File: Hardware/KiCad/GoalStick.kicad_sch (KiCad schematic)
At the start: 0 parts

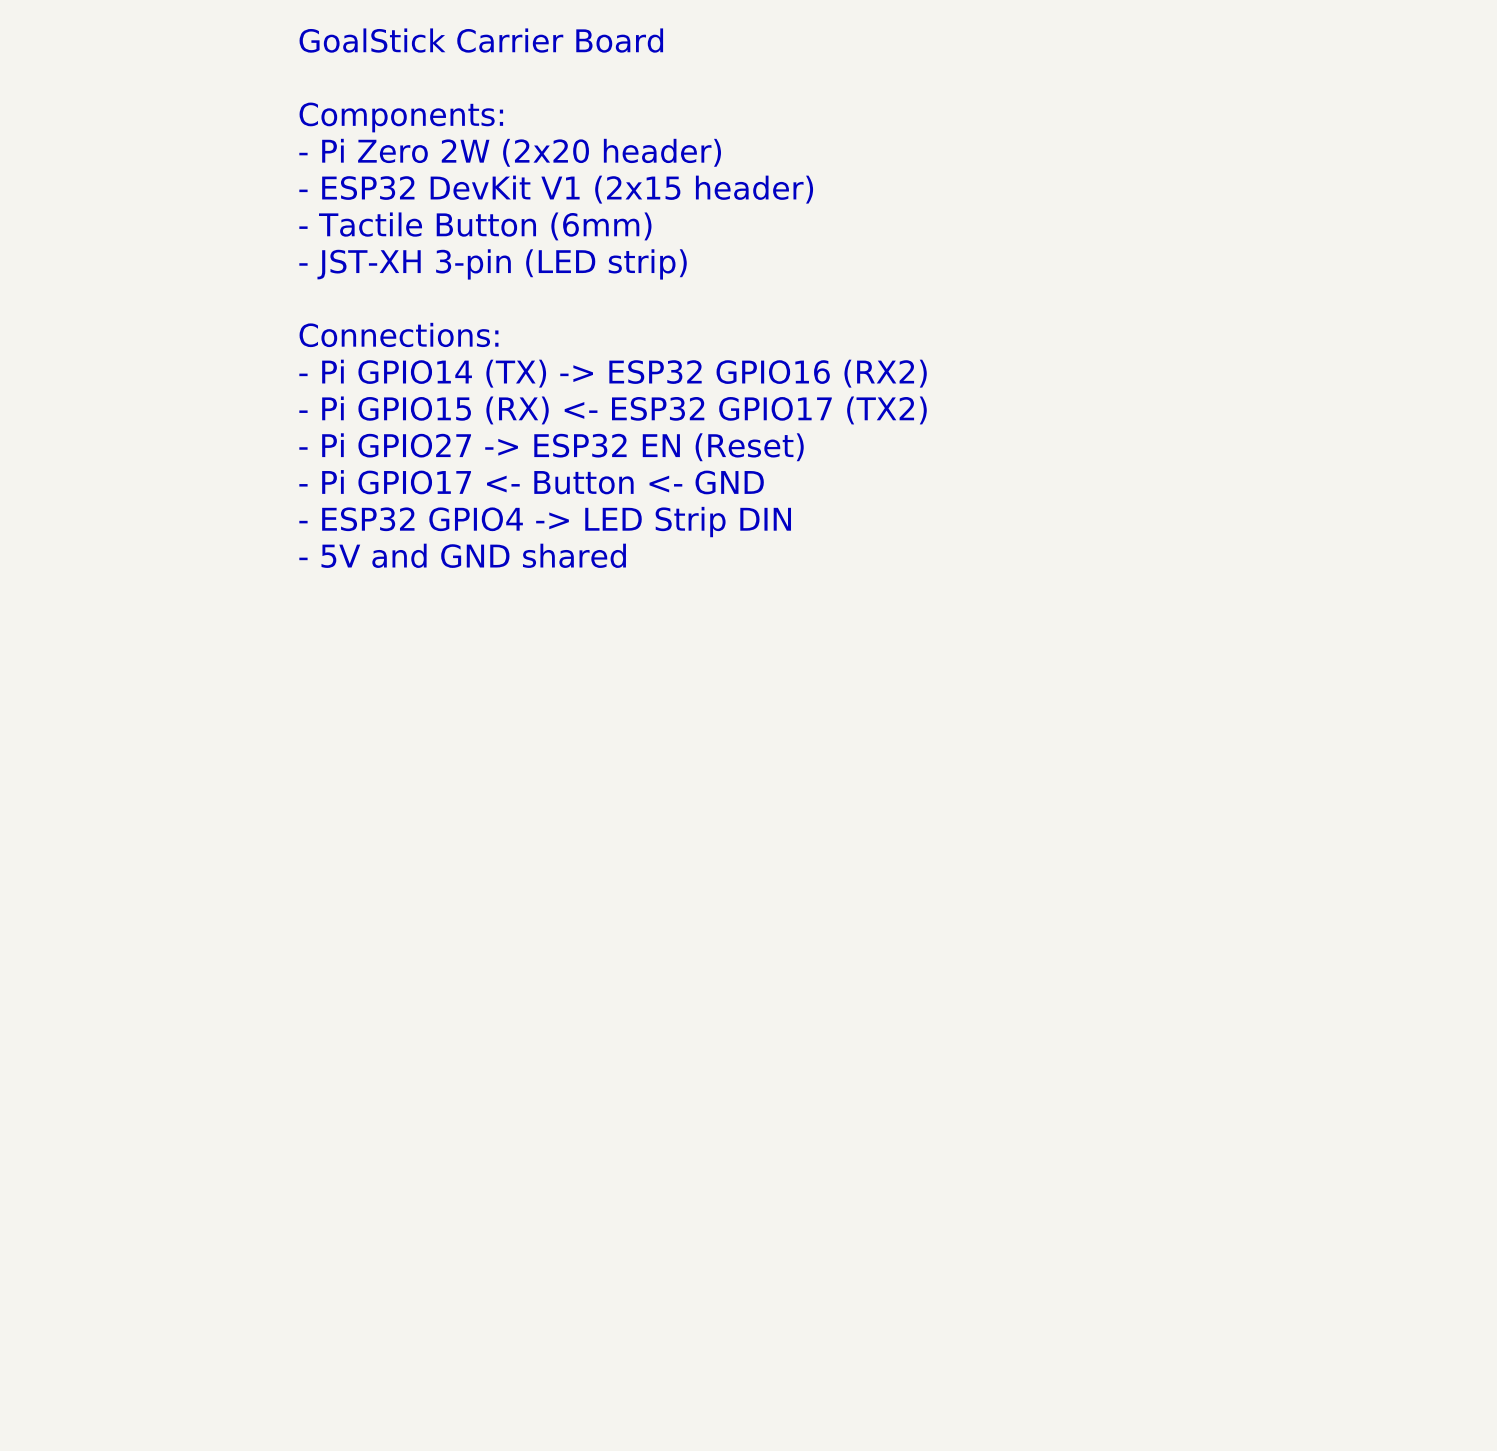
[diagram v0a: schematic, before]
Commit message: Add KiCad PCB design for GoalStick carrier board
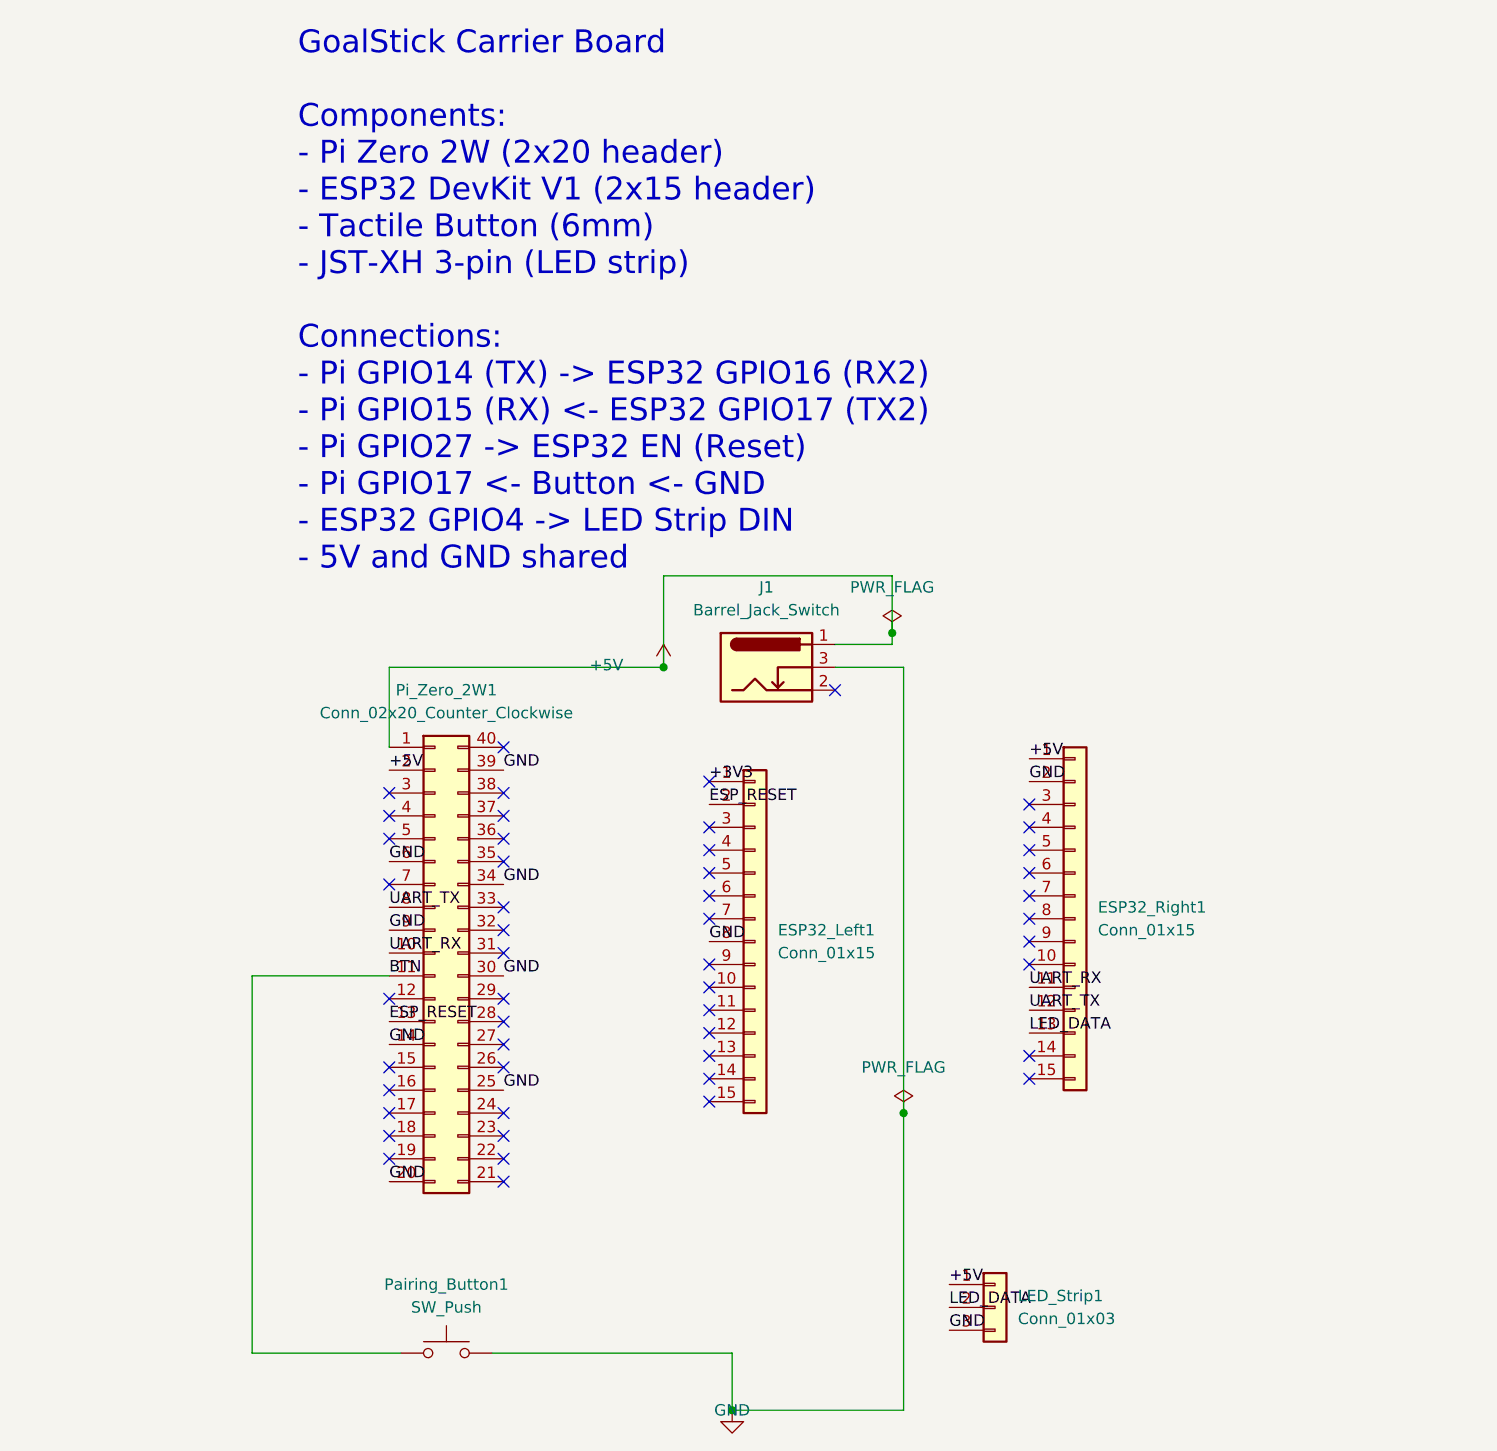
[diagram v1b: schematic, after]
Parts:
- added ESP32_Left1, ESP32_Right1: Conn_01x15, Connector_PinSocket_2.54mm:PinSocket_1x15_P2.54mm_Vertical, symbol Connector_Generic:Conn_01x15
- added J1: Barrel_Jack_Switch, Connector_BarrelJack:BarrelJack_Horizontal, symbol Connector:Barrel_Jack_Switch
- added LED_Strip1: Conn_01x03, Connector_JST:JST_XH_B3B-XH-A_1x03_P2.50mm_Vertical, symbol Connector_Generic:Conn_01x03
- added Pairing_Button1: SW_Push, Button_Switch_THT:SW_PUSH_6mm, symbol Switch:SW_Push
- added Pi_Zero_2W1: Conn_02x20_Counter_Clockwise, Connector_PinSocket_2.54mm:PinSocket_2x20_P2.54mm_Vertical, symbol Connector_Generic:Conn_02x20_Counter_Clockwise
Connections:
- new net +3V3: ESP32_Left1.1 (Pin_1)
- new net +5V: ESP32_Right1.1 (Pin_1), J1.1, LED_Strip1.1 (Pin_1), Pi_Zero_2W1.1 (Pin_1), Pi_Zero_2W1.2 (Pin_2)
- new net BTN: Pairing_Button1.1, Pi_Zero_2W1.11 (Pin_11)
- new net ESP_RESET: ESP32_Left1.2 (Pin_2), Pi_Zero_2W1.13 (Pin_13)
- new net GND: ESP32_Left1.8 (Pin_8), ESP32_Right1.2 (Pin_2), J1.3, LED_Strip1.3 (Pin_3), Pairing_Button1.2, Pi_Zero_2W1.14 (Pin_14), Pi_Zero_2W1.20 (Pin_20), Pi_Zero_2W1.25 (Pin_25), Pi_Zero_2W1.30 (Pin_30), Pi_Zero_2W1.34 (Pin_34), Pi_Zero_2W1.39 (Pin_39), Pi_Zero_2W1.6 (Pin_6), Pi_Zero_2W1.9 (Pin_9)
- new net LED_DATA: ESP32_Right1.13 (Pin_13), LED_Strip1.2 (Pin_2)
- new net UART_RX: ESP32_Right1.11 (Pin_11), Pi_Zero_2W1.10 (Pin_10)
- new net UART_TX: ESP32_Right1.12 (Pin_12), Pi_Zero_2W1.8 (Pin_8)
- no-connect marks 0 -> 50

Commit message: Add DEPLOYMENT.md, update ESP32 firmware for XIAO ESP32C3, add KiCad footprints
- Add DEPLOYMENT.md with hands-free installation instructions
- Update README.md to link to deployment guide
- Update ESP32 firmware for XIAO ESP32C3 (Serial1, pin mappings, startup delay)
- Add custom KiCad footprints for XIAO and Pi Zero 2W
- Update KiCad schematic and PCB layout
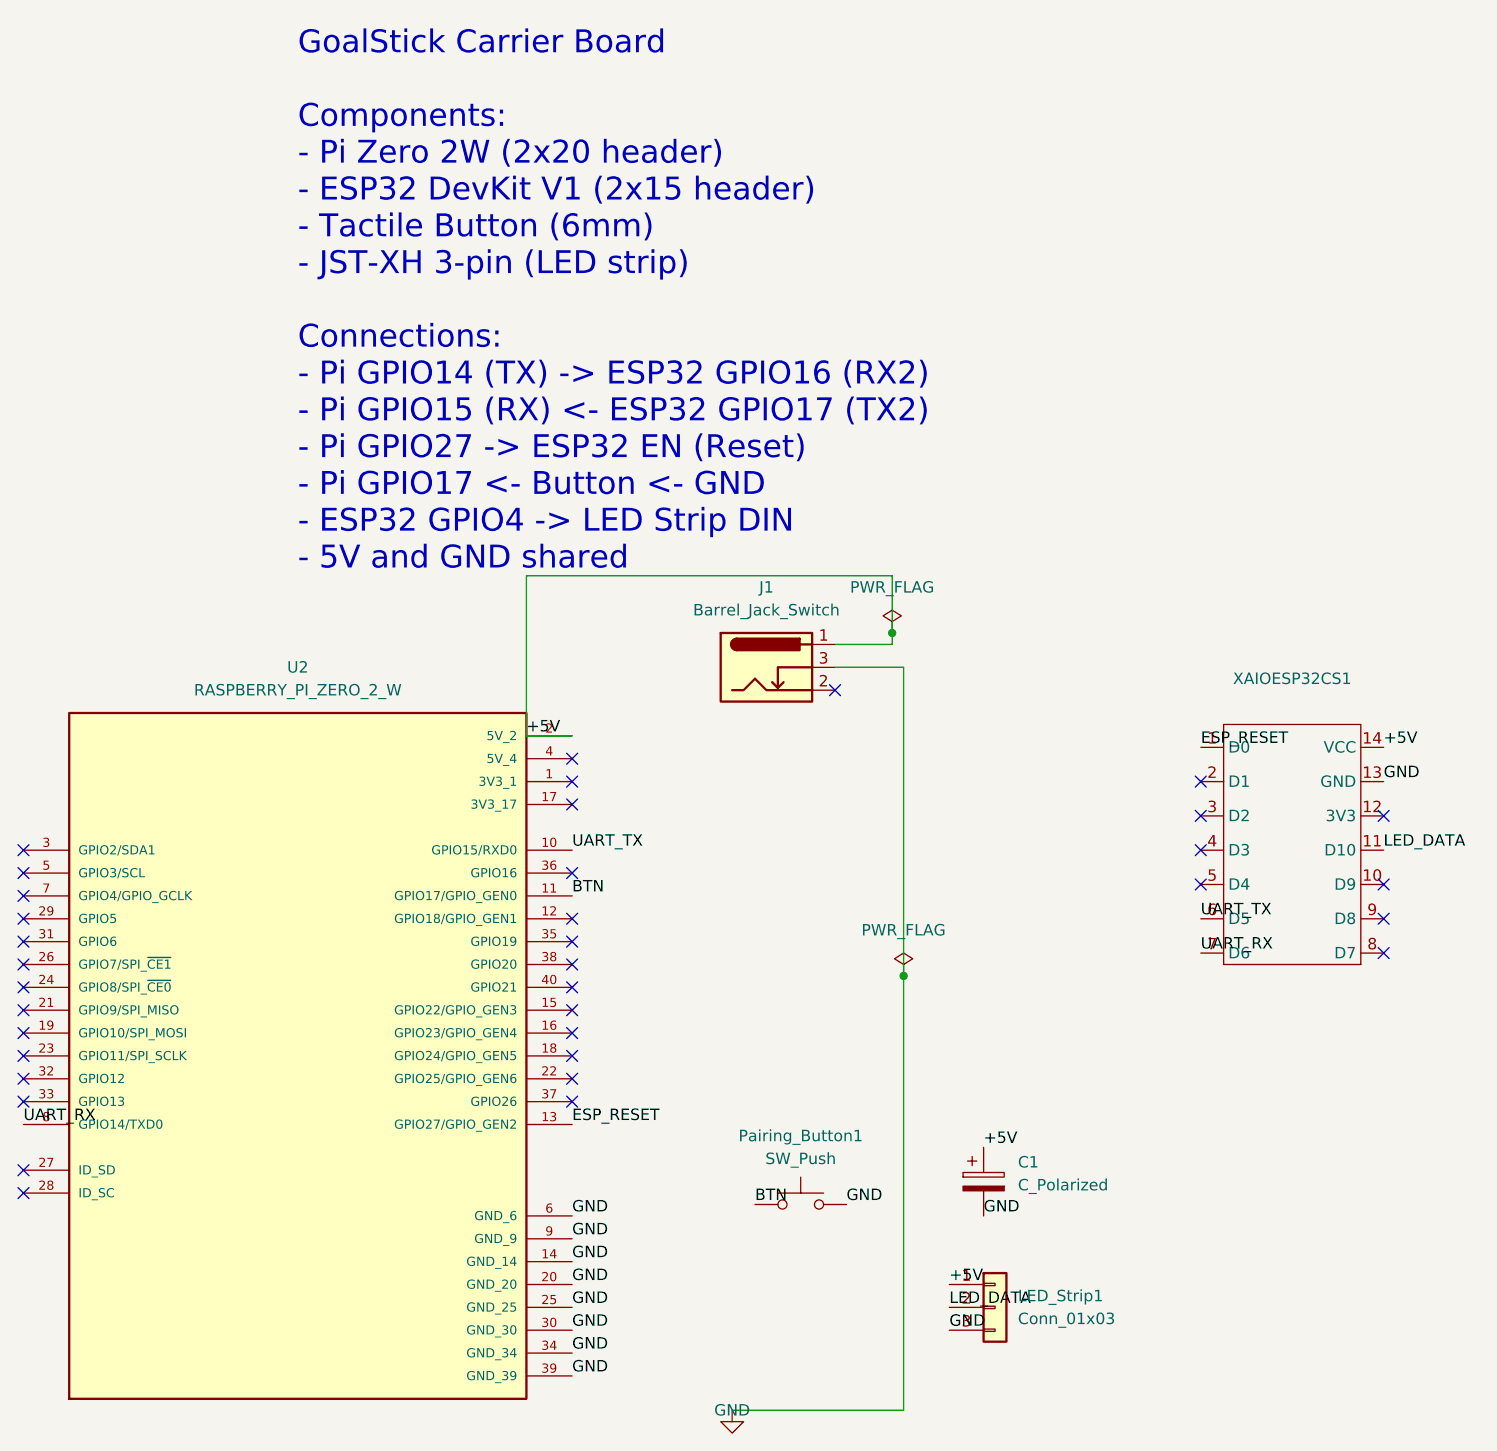
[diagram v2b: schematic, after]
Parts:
- removed ESP32_Left1, ESP32_Right1: Conn_01x15, Connector_PinSocket_2.54mm:PinSocket_1x15_P2.54mm_Vertical, symbol Connector_Generic:Conn_01x15
- removed Pi_Zero_2W1: Conn_02x20_Counter_Clockwise, Connector_PinSocket_2.54mm:PinSocket_2x20_P2.54mm_Vertical, symbol Connector_Generic:Conn_02x20_Counter_Clockwise
- added C1: C_Polarized, Capacitor_THT:CP_Radial_D8.0mm_P3.50mm, symbol Device:C_Polarized
- added U2: RASPBERRY_PI_ZERO_2_W, RASPBERRY_PI_ZERO_2_W:MODULE_RASPBERRY_PI_ZERO_2_W, symbol RASPBERRY_PI_ZERO_2_W:RASPBERRY_PI_ZERO_2_W
- added XAIOESP32CS1: ~, XAIO_Series:XIAO-ESP32-C3-DIP, symbol XAIO_ESP32C3:XAIOESP323CS
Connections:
- net +5V: now also C1.1, U2.2 (5V_2), XAIOESP32CS1.14 (VCC)
- net BTN: now also U2.11 (GPIO17/GPIO_GEN0)
- net ESP_RESET: now also U2.13 (GPIO27/GPIO_GEN2), XAIOESP32CS1.1 (D0)
- net GND: now also C1.2, U2.14 (GND_14), U2.20 (GND_20), U2.25 (GND_25), U2.30 (GND_30), U2.34 (GND_34), U2.39 (GND_39), U2.6 (GND_6), U2.9 (GND_9), XAIOESP32CS1.13 (GND)
- net LED_DATA: now also XAIOESP32CS1.11 (D10)
- net UART_RX: now also U2.8 (GPIO14/TXD0), XAIOESP32CS1.7 (D6)
- net UART_TX: now also U2.10 (GPIO15/RXD0), XAIOESP32CS1.6 (D5)
- no-connect marks 50 -> 36
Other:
- moved on the sheet: Pairing_Button1

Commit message: Update .gitignore and remove generated/local KiCad files from repo
Fixed bad routes on the Pi to ESP32 serial connections, updated SMD pads on the ESP32 to drilled holes.
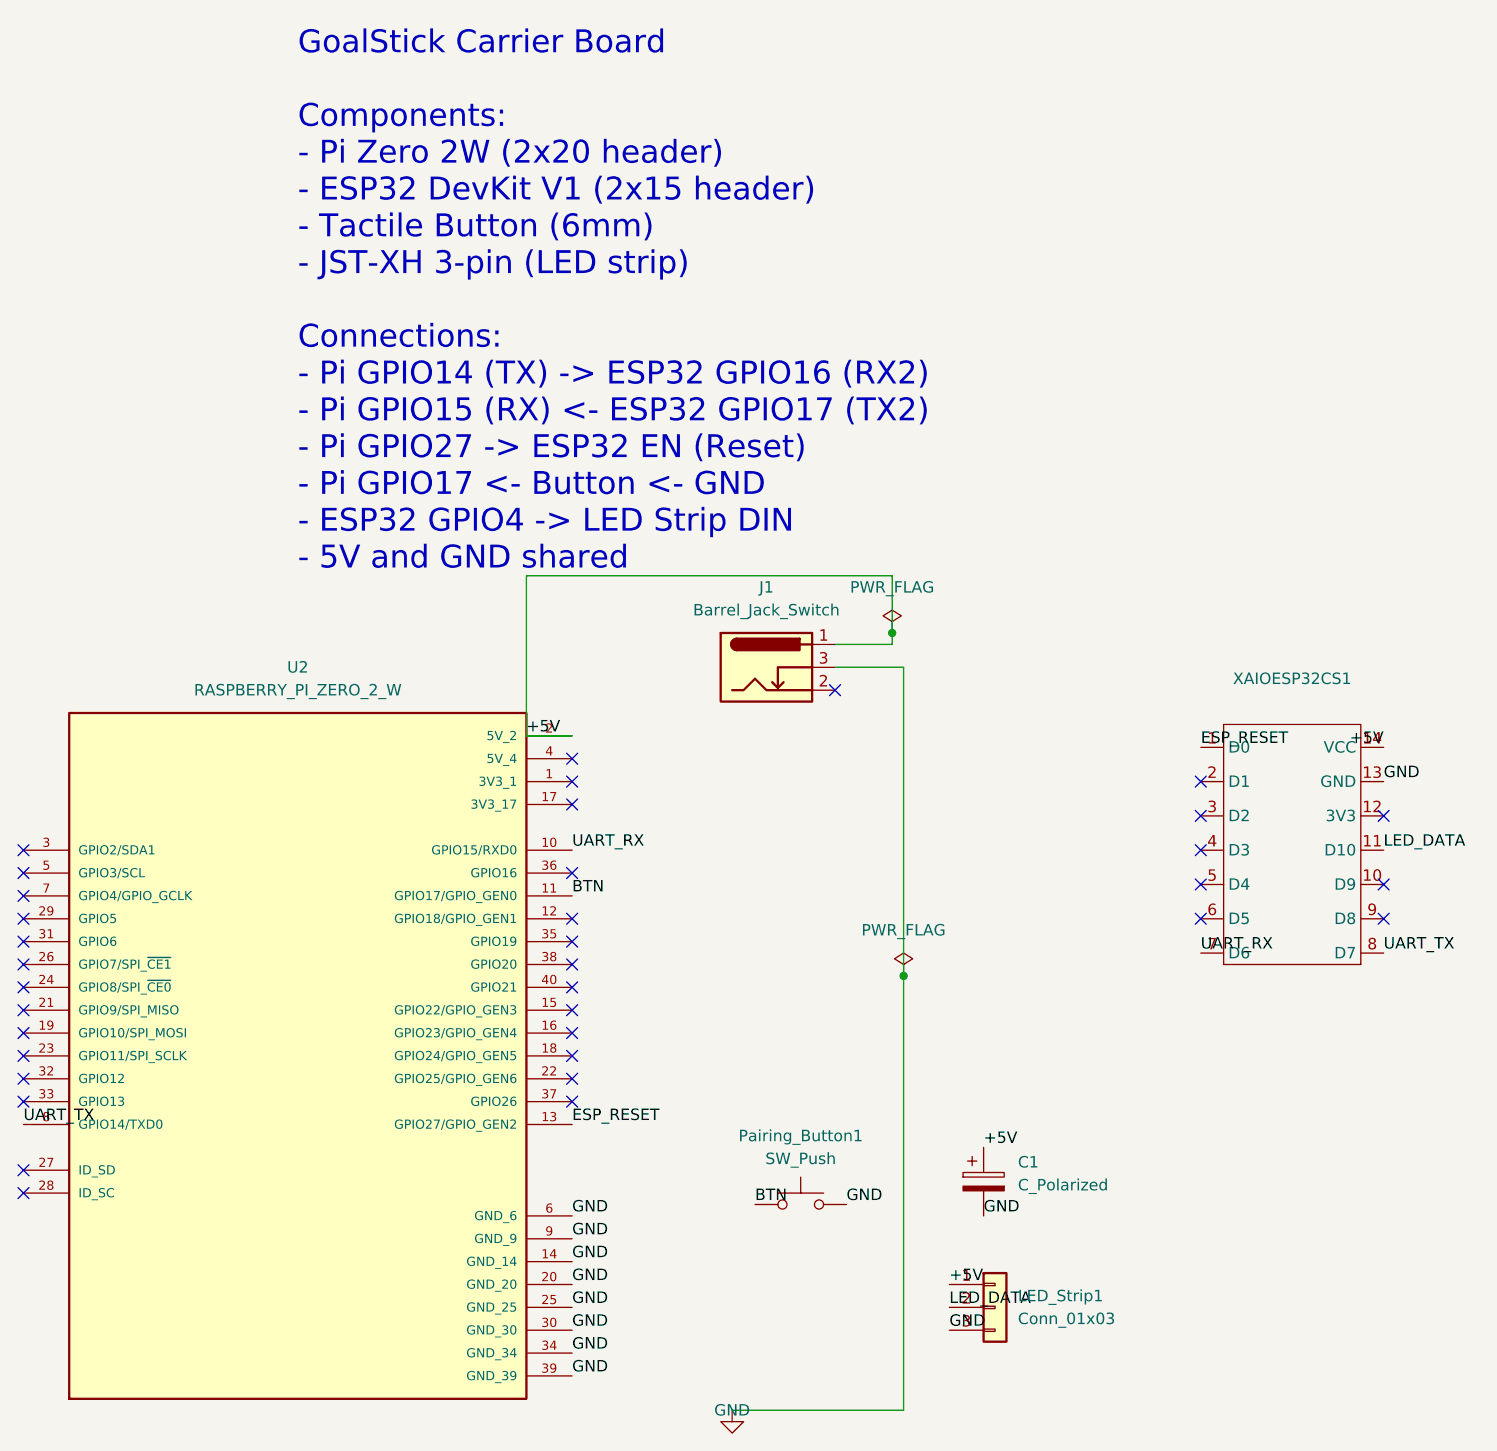
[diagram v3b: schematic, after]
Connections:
- net UART_RX: now also U2.10 (GPIO15/RXD0); no longer U2.8 (GPIO14/TXD0)
- net UART_TX: now also U2.8 (GPIO14/TXD0), XAIOESP32CS1.8 (D7); no longer U2.10 (GPIO15/RXD0), XAIOESP32CS1.6 (D5)
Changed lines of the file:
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@@
-	)
-	(no_connect
-		(at 171.45 123.19)
 	)
 	(no_connect
@@
 	)
 	(no_connect
+		(at 171.45 119.38)
+	)
+	(no_connect
 		(at 81.28 121.92)
 	)
@@
 	)
 	(no_connect
-		(at 171.45 119.38)
-	)
-	(no_connect
 		(at 20.32 116.84)
 	)
@@
 	(no_connect
 		(at 81.28 106.68)
+	)
+	(no_connect
+		(at 151.13 119.38)
 	)
 	(no_connect
@@
 	)
 	(label "UART_RX"
-		(at 20.32 142.24 0)
+		(at 81.28 111.76 0)
 		(effects
 			(font
@@
 	)
 	(label "UART_TX"
-		(at 151.13 119.38 0)
+		(at 171.45 123.19 0)
 		(effects
 			(font
@@
 	)
 	(label "UART_TX"
-		(at 81.28 111.76 0)
+		(at 20.32 142.24 0)
 		(effects
 			(font
@@
 	)
 	(label "+5V"
-		(at 171.45 100.33 0)
-		(effects
-			(font
-				(size 1.27 1.27)
-			)
-			(justify left bottom)
-		)
-	)
+		(at 171.45 100.33 180)
+		(effects
+			(font
+				(size 1.27 1.27)
+			)
+			(justify right bottom)
+		)
+	)
